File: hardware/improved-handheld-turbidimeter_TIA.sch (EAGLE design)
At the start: 11 parts

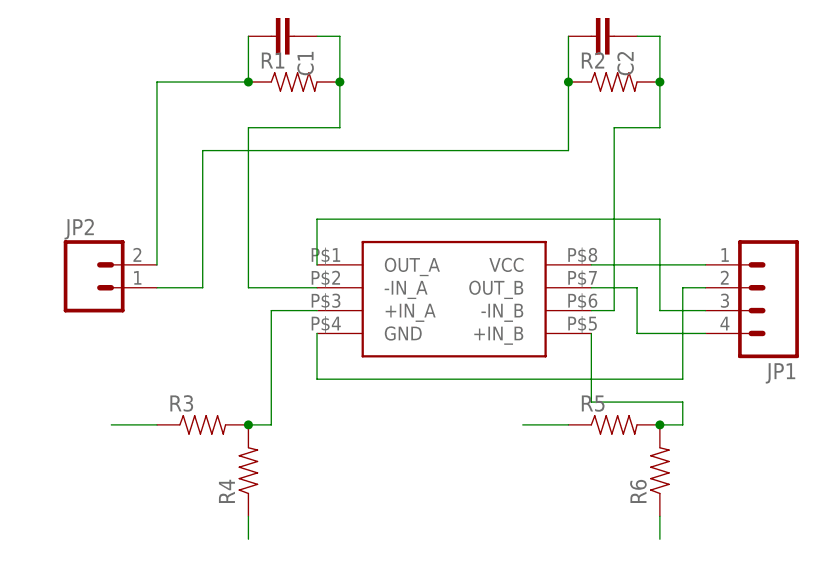
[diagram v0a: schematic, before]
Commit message: basic TIA board routed
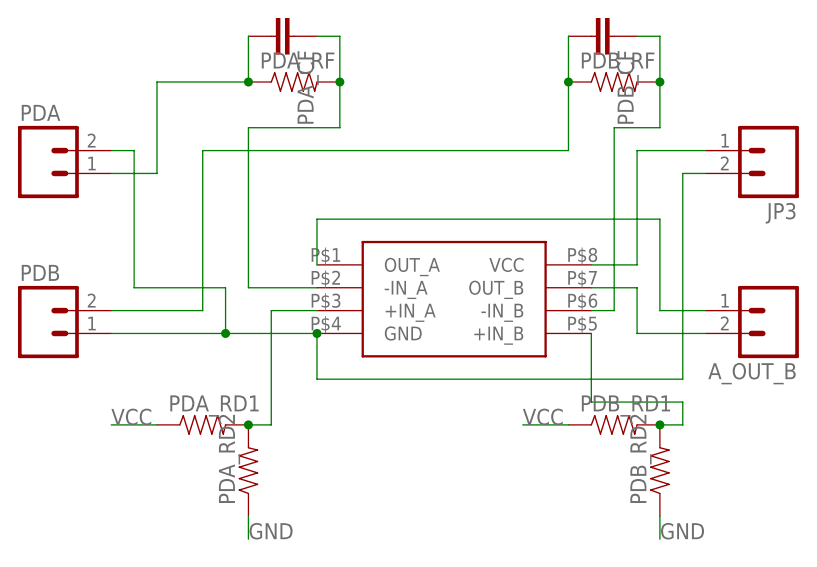
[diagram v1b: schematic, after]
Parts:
- removed JP1: (no value), SparkFun-Connectors:M04PTH
- removed JP2: (no value), SparkFun-Connectors:M02PTH
- added A_OUT_B, JP3, PDA, PDB: (no value), SparkFun-Connectors:M02PTH
- renumbered C1 to PDA_CF, C2 to PDB_CF, R1 to PDA_RF, R2 to PDB_RF, R3 to PDA_RD1, R4 to PDA_RD2, R5 to PDB_RD1, R6 to PDB_RD2
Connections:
- net GND: now also JP3.2, PDA.2, PDB.1; no longer JP1.2
- net N$1: now also PDA.1; no longer JP2.2
- net N$3: now also PDB.2; no longer JP2.1
- net OUTA: now also A_OUT_B.1; no longer JP1.3
- net OUTB: now also A_OUT_B.2; no longer JP1.4
- net VCC: now also JP3.1; no longer JP1.1
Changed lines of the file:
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@@
 <parts>
 <part name="U$1" library="awqua_eagle_library" deviceset="ADA4528" device=""/>
-<part name="R1" library="SparkFun-Passives" deviceset="RESISTOR" device="PTH-1/4W"/>
-<part name="R2" library="SparkFun-Passives" deviceset="RESISTOR" device="PTH-1/4W"/>
-<part name="C1" library="SparkFun-Passives" deviceset="CAP" device="PTH1"/>
-<part name="C2" library="SparkFun-Passives" deviceset="CAP" device="PTH1"/>
-<part name="JP1" library="SparkFun-Connectors" deviceset="M04" device="PTH"/>
-<part name="R3" library="SparkFun-Passives" deviceset="RESISTOR" device="PTH-1/4W"/>
-<part name="R4" library="SparkFun-Passives" deviceset="RESISTOR" device="PTH-1/4W"/>
-<part name="R5" library="SparkFun-Passives" deviceset="RESISTOR" device="PTH-1/4W"/>
-<part name="R6" library="SparkFun-Passives" deviceset="RESISTOR" device="PTH-1/4W"/>
-<part name="JP2" library="SparkFun-Connectors" deviceset="M02" device="PTH"/>
+<part name="PDA_RF" library="SparkFun-Passives" deviceset="RESISTOR" device="PTH-1/4W"/>
+<part name="PDB_RF" library="SparkFun-Passives" deviceset="RESISTOR" device="PTH-1/4W"/>
+<part name="PDA_CF" library="SparkFun-Passives" deviceset="CAP" device="PTH1"/>
+<part name="PDB_CF" library="SparkFun-Passives" deviceset="CAP" device="PTH1"/>
+<part name="PDA_RD1" library="SparkFun-Passives" deviceset="RESISTOR" device="PTH-1/4W"/>
+<part name="PDA_RD2" library="SparkFun-Passives" deviceset="RESISTOR" device="PTH-1/4W"/>
+<part name="PDB_RD1" library="SparkFun-Passives" deviceset="RESISTOR" device="PTH-1/4W"/>
+<part name="PDB_RD2" library="SparkFun-Passives" deviceset="RESISTOR" device="PTH-1/4W"/>
+<part name="PDA" library="SparkFun-Connectors" deviceset="M02" device="PTH"/>
+<part name="PDB" library="SparkFun-Connectors" deviceset="M02" device="PTH"/>
+<part name="JP3" library="SparkFun-Connectors" deviceset="M02" device="PTH"/>
+<part name="A_OUT_B" library="SparkFun-Connectors" deviceset="M02" device="PTH"/>
 </parts>
 <sheets>
@@
 <instances>
 <instance part="U$1" gate="G$1" x="25.4" y="20.32"/>
-<instance part="R1" gate="G$1" x="17.78" y="50.8"/>
-<instance part="R2" gate="G$1" x="53.34" y="50.8"/>
-<instance part="C1" gate="G$1" x="15.24" y="55.88" rot="R270"/>
-<instance part="C2" gate="G$1" x="50.8" y="55.88" rot="R270"/>
-<instance part="JP1" gate="G$1" x="68.58" y="27.94" rot="R180"/>
-<instance part="R3" gate="G$1" x="7.62" y="12.7"/>
-<instance part="R4" gate="G$1" x="12.7" y="7.62" rot="R90"/>
-<instance part="R5" gate="G$1" x="53.34" y="12.7"/>
-<instance part="R6" gate="G$1" x="58.42" y="7.62" rot="R90"/>
-<instance part="JP2" gate="G$1" x="-5.08" y="27.94"/>
+<instance part="PDA_RF" gate="G$1" x="17.78" y="50.8"/>
+<instance part="PDB_RF" gate="G$1" x="53.34" y="50.8"/>
+<instance part="PDA_CF" gate="G$1" x="15.24" y="55.88" rot="R270"/>
+<instance part="PDB_CF" gate="G$1" x="50.8" y="55.88" rot="R270"/>
+<instance part="PDA_RD1" gate="G$1" x="7.62" y="12.7"/>
+<instance part="PDA_RD2" gate="G$1" x="12.7" y="7.62" rot="R90"/>
+<instance part="PDB_RD1" gate="G$1" x="53.34" y="12.7"/>
+<instance part="PDB_RD2" gate="G$1" x="58.42" y="7.62" rot="R90"/>
+<instance part="PDA" gate="G$1" x="-10.16" y="40.64"/>
+<instance part="PDB" gate="G$1" x="-10.16" y="22.86"/>
+<instance part="JP3" gate="G$1" x="71.12" y="43.18" rot="R180"/>
+<instance part="A_OUT_B" gate="G$1" x="71.12" y="25.4" rot="R180"/>
 </instances>
 <busses>
@@
 <net name="VCC" class="0">
 <segment>
-<pinref part="U$1" gate="G$1" pin="VCC"/>
-<pinref part="JP1" gate="G$1" pin="1"/>
-<wire x1="50.8" y1="30.48" x2="63.5" y2="30.48" width="0.1524" layer="91"/>
+<pinref part="PDA_RD1" gate="G$1" pin="1"/>
+<wire x1="-2.54" y1="12.7" x2="2.54" y2="12.7" width="0.1524" layer="91"/>
+<label x="-2.54" y="12.7" size="1.778" layer="95"/>
 </segment>
 <segment>
-<pinref part="R3" gate="G$1" pin="1"/>
-<wire x1="-2.54" y1="12.7" x2="2.54" y2="12.7" width="0.1524" layer="91"/>
+<pinref part="PDB_RD1" gate="G$1" pin="1"/>
+<wire x1="43.18" y1="12.7" x2="48.26" y2="12.7" width="0.1524" layer="91"/>
+<label x="43.18" y="12.7" size="1.778" layer="95"/>
 </segment>
 <segment>
-<pinref part="R5" gate="G$1" pin="1"/>
-<wire x1="43.18" y1="12.7" x2="48.26" y2="12.7" width="0.1524" layer="91"/>
+<pinref part="U$1" gate="G$1" pin="VCC"/>
+<wire x1="50.8" y1="30.48" x2="55.88" y2="30.48" width="0.1524" layer="91"/>
+<wire x1="55.88" y1="30.48" x2="55.88" y2="43.18" width="0.1524" layer="91"/>
+<pinref part="JP3" gate="G$1" pin="1"/>
+<wire x1="55.88" y1="43.18" x2="63.5" y2="43.18" width="0.1524" layer="91"/>
 </segment>
 </net>
@@
 <wire x1="50.8" y1="27.94" x2="55.88" y2="27.94" width="0.1524" layer="91"/>
 <wire x1="55.88" y1="27.94" x2="55.88" y2="22.86" width="0.1524" layer="91"/>
-<pinref part="JP1" gate="G$1" pin="4"/>
 <wire x1="55.88" y1="22.86" x2="63.5" y2="22.86" width="0.1524" layer="91"/>
+<pinref part="A_OUT_B" gate="G$1" pin="2"/>
 </segment>
 </net>
@@
 <wire x1="20.32" y1="22.86" x2="20.32" y2="17.78" width="0.1524" layer="91"/>
 <wire x1="20.32" y1="17.78" x2="60.96" y2="17.78" width="0.1524" layer="91"/>
-<wire x1="60.96" y1="17.78" x2="60.96" y2="27.94" width="0.1524" layer="91"/>
-<pinref part="JP1" gate="G$1" pin="2"/>
-<wire x1="60.96" y1="27.94" x2="63.5" y2="27.94" width="0.1524" layer="91"/>
+<wire x1="20.32" y1="22.86" x2="10.16" y2="22.86" width="0.1524" layer="91"/>
+<junction x="20.32" y="22.86"/>
+<wire x1="10.16" y1="27.94" x2="10.16" y2="22.86" width="0.1524" layer="91"/>
+<junction x="10.16" y="22.86"/>
+<pinref part="PDA" gate="G$1" pin="2"/>
+<wire x1="-2.54" y1="43.18" x2="0" y2="43.18" width="0.1524" layer="91"/>
+<wire x1="0" y1="43.18" x2="0" y2="27.94" width="0.1524" layer="91"/>
+<wire x1="0" y1="27.94" x2="10.16" y2="27.94" width="0.1524" layer="91"/>
+<pinref part="PDB" gate="G$1" pin="1"/>
+<wire x1="10.16" y1="22.86" x2="-2.54" y2="22.86" width="0.1524" layer="91"/>
+<wire x1="60.96" y1="17.78" x2="60.96" y2="40.64" width="0.1524" layer="91"/>
+<pinref part="JP3" gate="G$1" pin="2"/>
+<wire x1="60.96" y1="40.64" x2="63.5" y2="40.64" width="0.1524" layer="91"/>
 </segment>
 <segment>
-<pinref part="R4" gate="G$1" pin="1"/>
+<pinref part="PDA_RD2" gate="G$1" pin="1"/>
 <wire x1="12.7" y1="0" x2="12.7" y2="2.54" width="0.1524" layer="91"/>
+<label x="12.7" y="0" size="1.778" layer="95"/>
 </segment>
 <segment>
-<pinref part="R6" gate="G$1" pin="1"/>
+<pinref part="PDB_RD2" gate="G$1" pin="1"/>
 <wire x1="58.42" y1="0" x2="58.42" y2="2.54" width="0.1524" layer="91"/>
+<label x="58.42" y="0" size="1.778" layer="95"/>
 </segment>
 </net>
@@
 <wire x1="20.32" y1="35.56" x2="58.42" y2="35.56" width="0.1524" layer="91"/>
 <wire x1="58.42" y1="35.56" x2="58.42" y2="25.4" width="0.1524" layer="91"/>
-<pinref part="JP1" gate="G$1" pin="3"/>
 <wire x1="58.42" y1="25.4" x2="63.5" y2="25.4" width="0.1524" layer="91"/>
+<pinref part="A_OUT_B" gate="G$1" pin="1"/>
 </segment>
 </net>
 <net name="N$5" class="0">
 <segment>
-<pinref part="R3" gate="G$1" pin="2"/>
-<pinref part="R4" gate="G$1" pin="2"/>
+<pinref part="PDA_RD1" gate="G$1" pin="2"/>
+<pinref part="PDA_RD2" gate="G$1" pin="2"/>
 <wire x1="15.24" y1="12.7" x2="12.7" y2="12.7" width="0.1524" layer="91"/>
 <junction x="12.7" y="12.7"/>
@@
 <net name="N$6" class="0">
 <segment>
-<pinref part="R5" gate="G$1" pin="2"/>
-<pinref part="R6" gate="G$1" pin="2"/>
+<pinref part="PDB_RD1" gate="G$1" pin="2"/>
+<pinref part="PDB_RD2" gate="G$1" pin="2"/>
 <wire x1="60.96" y1="12.7" x2="58.42" y2="12.7" width="0.1524" layer="91"/>
 <junction x="58.42" y="12.7"/>
@@
 <net name="N$1" class="0">
 <segment>
-<pinref part="C1" gate="G$1" pin="2"/>
-<pinref part="R1" gate="G$1" pin="1"/>
+<pinref part="PDA_CF" gate="G$1" pin="2"/>
+<pinref part="PDA_RF" gate="G$1" pin="1"/>
 <wire x1="12.7" y1="55.88" x2="12.7" y2="50.8" width="0.1524" layer="91"/>
-<pinref part="JP2" gate="G$1" pin="2"/>
-<wire x1="2.54" y1="30.48" x2="2.54" y2="50.8" width="0.1524" layer="91"/>
 <wire x1="2.54" y1="50.8" x2="12.7" y2="50.8" width="0.1524" layer="91"/>
 <junction x="12.7" y="50.8"/>
+<wire x1="2.54" y1="50.8" x2="2.54" y2="40.64" width="0.1524" layer="91"/>
+<pinref part="PDA" gate="G$1" pin="1"/>
+<wire x1="2.54" y1="40.64" x2="-2.54" y2="40.64" width="0.1524" layer="91"/>
 </segment>
 </net>
 <net name="N$2" class="0">
 <segment>
-<pinref part="C1" gate="G$1" pin="1"/>
-<pinref part="R1" gate="G$1" pin="2"/>
+<pinref part="PDA_CF" gate="G$1" pin="1"/>
+<pinref part="PDA_RF" gate="G$1" pin="2"/>
 <wire x1="20.32" y1="55.88" x2="22.86" y2="55.88" width="0.1524" layer="91"/>
 <wire x1="22.86" y1="55.88" x2="22.86" y2="50.8" width="0.1524" layer="91"/>
@@
 <net name="N$3" class="0">
 <segment>
-<pinref part="C2" gate="G$1" pin="2"/>
-<pinref part="R2" gate="G$1" pin="1"/>
+<pinref part="PDB_CF" gate="G$1" pin="2"/>
+<pinref part="PDB_RF" gate="G$1" pin="1"/>
 <wire x1="48.26" y1="55.88" x2="48.26" y2="50.8" width="0.1524" layer="91"/>
-<pinref part="JP2" gate="G$1" pin="1"/>
-<wire x1="2.54" y1="27.94" x2="7.62" y2="27.94" width="0.1524" layer="91"/>
-<wire x1="7.62" y1="27.94" x2="7.62" y2="43.18" width="0.1524" layer="91"/>
+<wire x1="7.62" y1="25.4" x2="7.62" y2="43.18" width="0.1524" layer="91"/>
 <wire x1="7.62" y1="43.18" x2="48.26" y2="43.18" width="0.1524" layer="91"/>
 <wire x1="48.26" y1="43.18" x2="48.26" y2="50.8" width="0.1524" layer="91"/>
 <junction x="48.26" y="50.8"/>
+<pinref part="PDB" gate="G$1" pin="2"/>
+<wire x1="7.62" y1="25.4" x2="-2.54" y2="25.4" width="0.1524" layer="91"/>
 </segment>
 </net>
 <net name="N$4" class="0">
 <segment>
-<pinref part="C2" gate="G$1" pin="1"/>
-<pinref part="R2" gate="G$1" pin="2"/>
+<pinref part="PDB_CF" gate="G$1" pin="1"/>
+<pinref part="PDB_RF" gate="G$1" pin="2"/>
 <wire x1="55.88" y1="55.88" x2="58.42" y2="55.88" width="0.1524" layer="91"/>
 <wire x1="58.42" y1="55.88" x2="58.42" y2="50.8" width="0.1524" layer="91"/>

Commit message: upd
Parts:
- removed U$1: ADA4528, awqua_eagle_library:ADA4528
- added U$2: ADA4528-2, awqua_eagle_library:ADA4528-2
- PDA_CF, PDB_CF: device SparkFun-Passives:CAPPTH1 -> SparkFun-Passives:CAP0603-CAP
- PDA_RD1, PDA_RD2, PDA_RF, PDB_RD1, PDB_RD2, PDB_RF: device SparkFun-Passives:RESISTORPTH-1/4W -> SparkFun-Passives:RESISTOR0603-RES
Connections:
- net GND: now also U$2.GND; no longer U$1.GND
- net N$2: now also U$2.-IN_A; no longer U$1.-IN_A
- net N$4: now also U$2.-IN_B; no longer U$1.-IN_B
- net N$5: now also U$2.+IN_A; no longer U$1.+IN_A
- net N$6: now also U$2.+IN_B; no longer U$1.+IN_B
- net OUTA: now also U$2.OUT_A; no longer U$1.OUT_A
- net OUTB: now also U$2.OUT_B; no longer U$1.OUT_B
- net VCC: now also U$2.VCC; no longer U$1.VCC
